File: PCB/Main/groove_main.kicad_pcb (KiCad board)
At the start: 2 copper layers, 214 x 99 mm, 118 parts, among them J1 Left_X, J10 Left_Y, J11 Right_X, J12 Right_Y, J13 SW, J14 SW, J15 V, J16 LED, J17 LED, J18 G, J19 V, J2 Left_Y, J20 LED, J21 LED, J22 G, J23 SW, J24 SW, J25 V, J26 V, J27 G, J28 G, J29 HAP, J3 Right_X, J30 V, J31 HAP, J32 V, J4 Right_Y, J5 Left_X, J6 Left_Y, J7 Right_X, J8 Right_Y, J9 Left_X, Q1 AO3400A, Q2 AO3400A, SW1 SWITCH_SPST, SW2 SWITCH_SPST, SW3 SWITCH_SPST, SW4 SWITCH_SPST, SW5 SWITCH_SPST, U1 Pico, U2 CD4052B, U3 LM4040DBZ-3

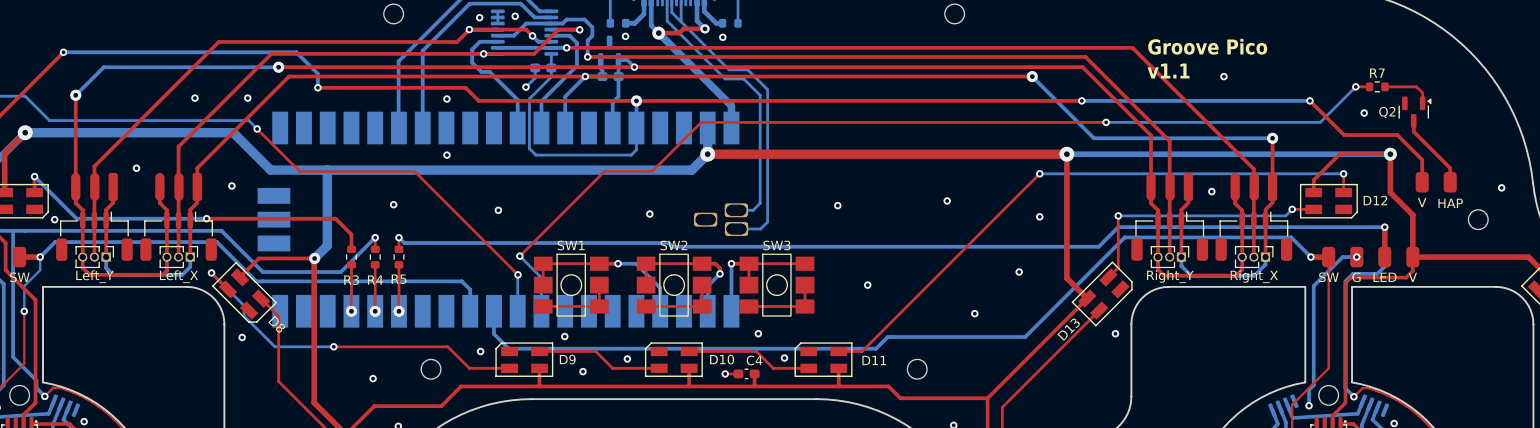
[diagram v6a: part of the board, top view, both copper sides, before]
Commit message: Optimize smd jst connector footprint
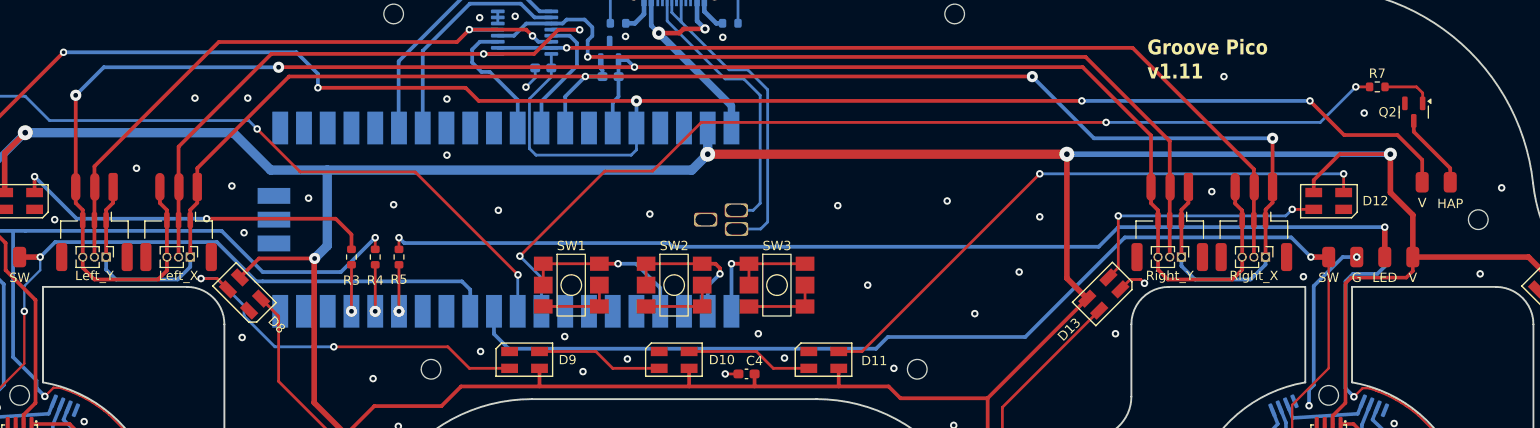
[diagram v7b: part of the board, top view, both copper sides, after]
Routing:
- net GND: track 93.2 -> 96.4 mm, vias 86 -> 92
- net Net-(D8-Out): track 39.2 -> 41.0 mm
- net GNDREF: track 194.3 -> 195.2 mm
- net +3.3VADC: track 200.2 -> 200.9 mm
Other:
- board text added: "Groove Pico v1.11"
- board text removed: "Groove Pico v1.1"

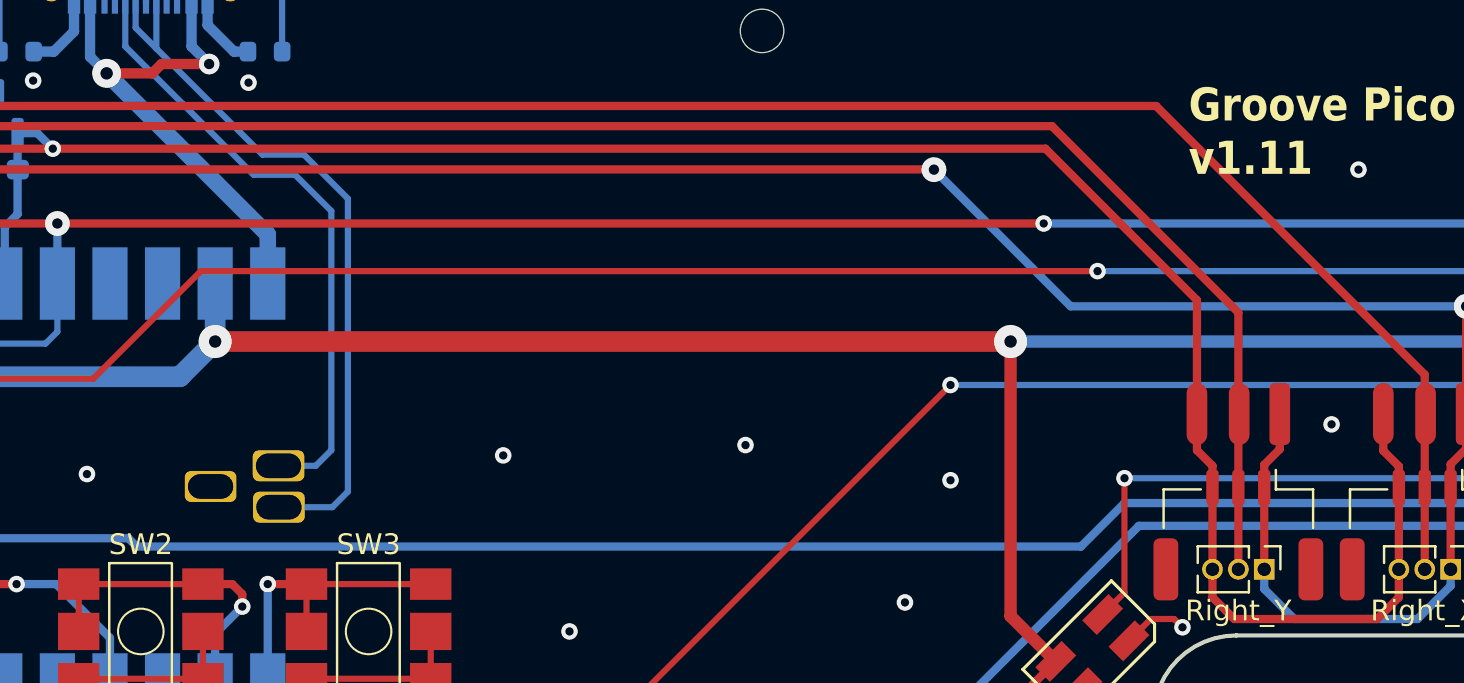
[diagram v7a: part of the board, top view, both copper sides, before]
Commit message: PCB v1.2 (easier USB soldering holes)
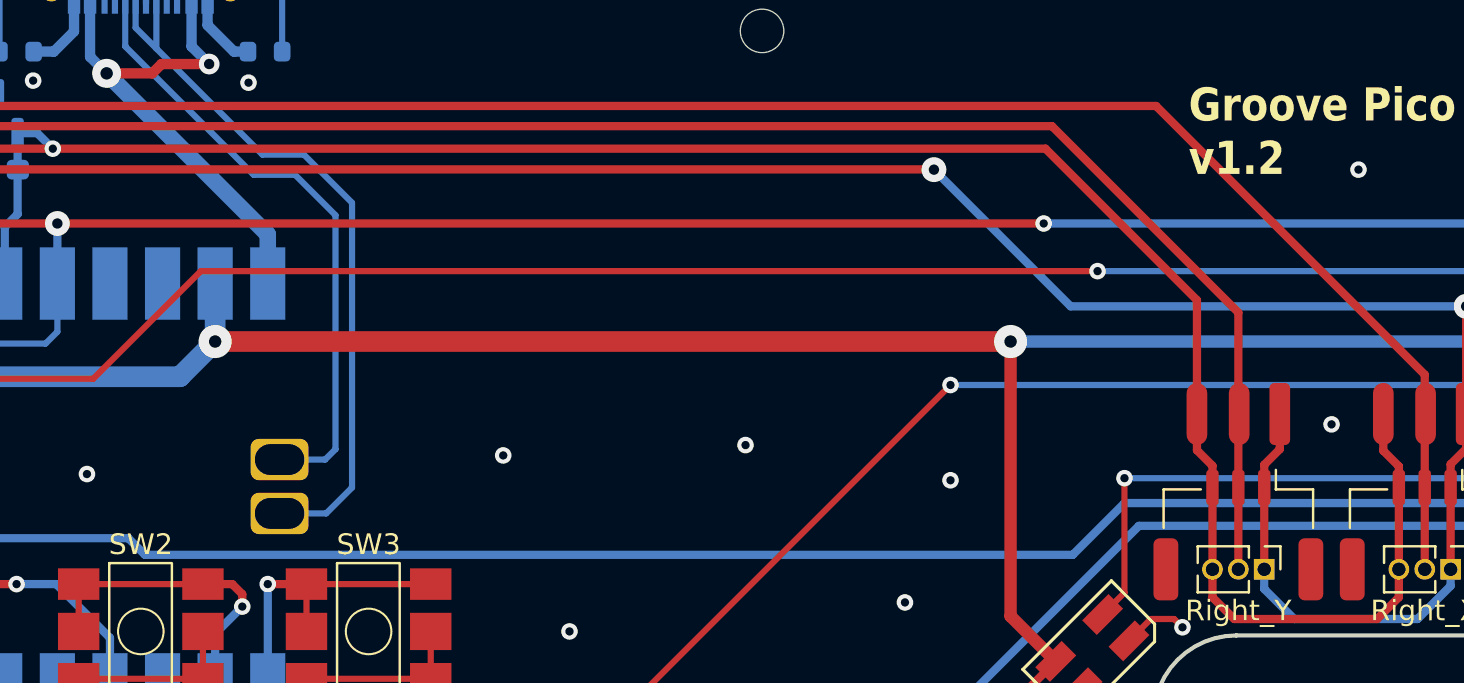
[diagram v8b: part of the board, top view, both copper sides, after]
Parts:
- U1: value Pico -> PiPico
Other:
- board text added: "Groove Pico v1.2"
- board text removed: "Groove Pico v1.11"
